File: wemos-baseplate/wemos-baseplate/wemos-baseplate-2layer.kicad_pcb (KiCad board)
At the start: 4 copper layers, 138.1 x 57 mm, 22 parts, among them J1 Conn_02x16_Odd_Even, J10 Conn_01x04, J11 Conn_01x04, J12 Conn_01x04, J13 Conn_01x04, J14 Conn_01x04, J15 Conn_01x04, J2 Conn_02x16_Odd_Even, J3 Conn_01x04, J4 Conn_01x04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

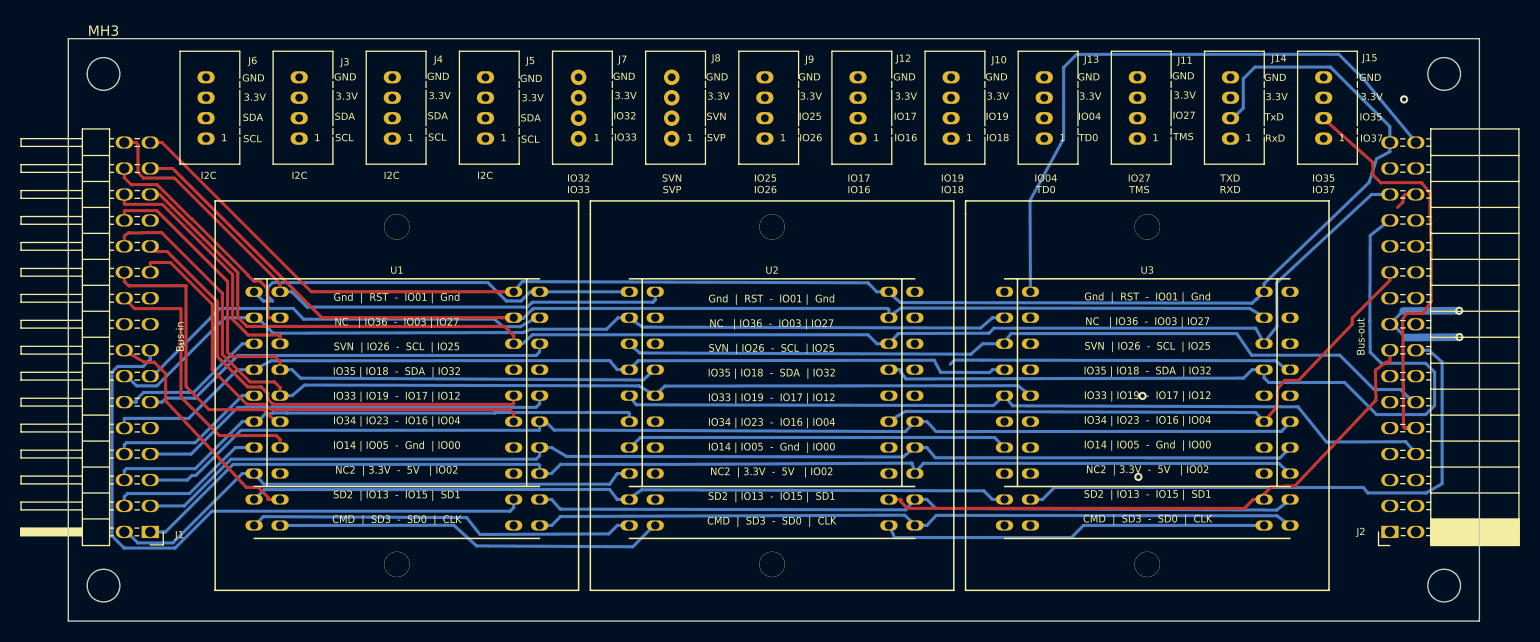
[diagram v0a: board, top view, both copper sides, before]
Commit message: finished 2 layer version
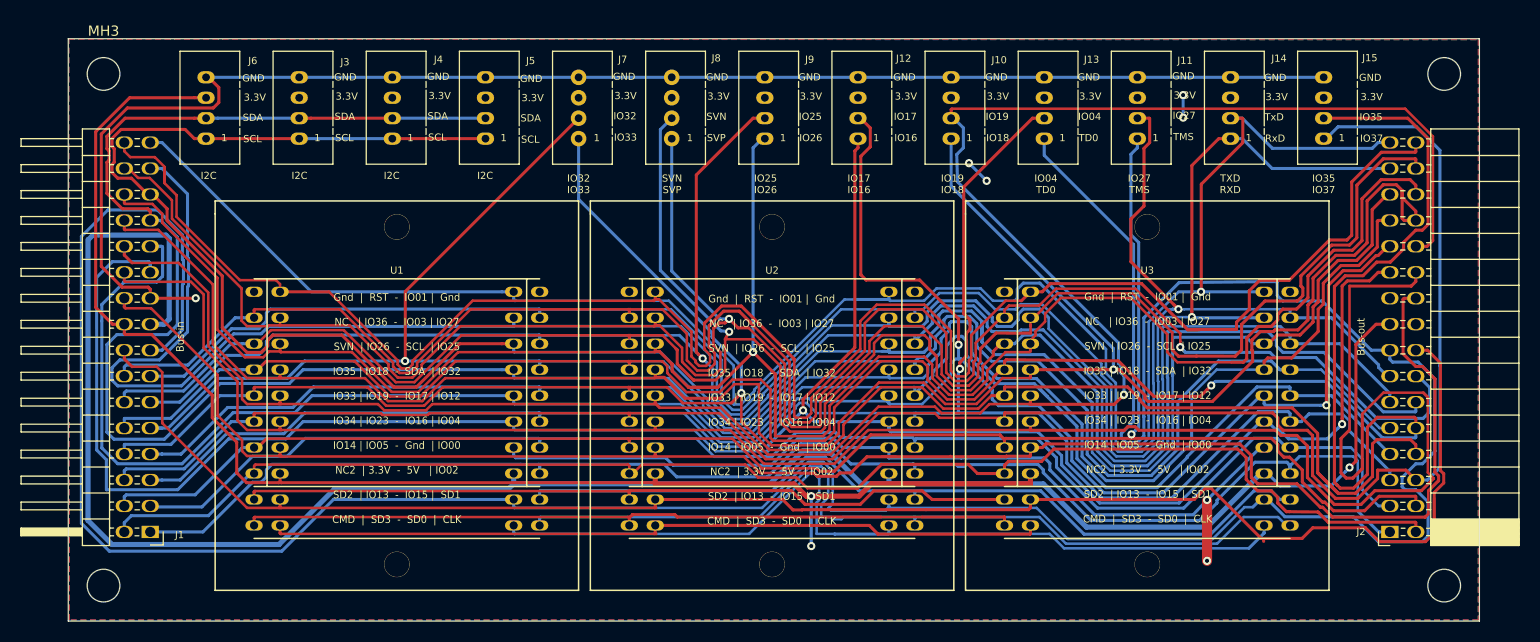
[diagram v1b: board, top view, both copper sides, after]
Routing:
- net /GND: track 40.8 -> 237.8 mm
- net /SVP: track 25.0 -> 213.0 mm, vias 0 -> 1
- net /5V: track 15.4 -> 199.4 mm, vias 2 -> 1
- net /TD0: track 122.4 -> 302.9 mm
- net /IO26: track 28.0 -> 205.9 mm, vias 0 -> 1
- net /IO17: track 69.8 -> 227.9 mm, vias 0 -> 2
- net /3.3V: track 0.25 -> 145.8 mm, vias 0 -> 6
- net /IO25: track 53.1 -> 193.5 mm, vias 0 -> 1
- net /IO18: track 64.6 -> 204.4 mm, vias 0 -> 1
- net /IO23: track 68.3 -> 201.5 mm
- net /IO27: track 53.9 -> 187.1 mm, vias 0 -> 1
- net /SVN: track 96.5 -> 211.2 mm, vias 0 -> 1
- net /IO19: track 101.8 -> 213.6 mm, vias 0 -> 1
- net /IO16: track 105.0 -> 213.9 mm, vias 0 -> 2
- net /IO32: track 83.7 -> 190.3 mm, vias 0 -> 1
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- added copper zone on F.Cu, net /3.3V
- added copper zone on B.Cu, net /GND
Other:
- copper layers 4 -> 2
- net class Default: trace_width 0.25 -> 0.3
